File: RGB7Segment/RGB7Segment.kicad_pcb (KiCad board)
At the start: 2 copper layers, 38.5 x 25.5 mm, 21 parts, among them J1 Conn_01x02_Socket, J2 Conn_01x02_Socket

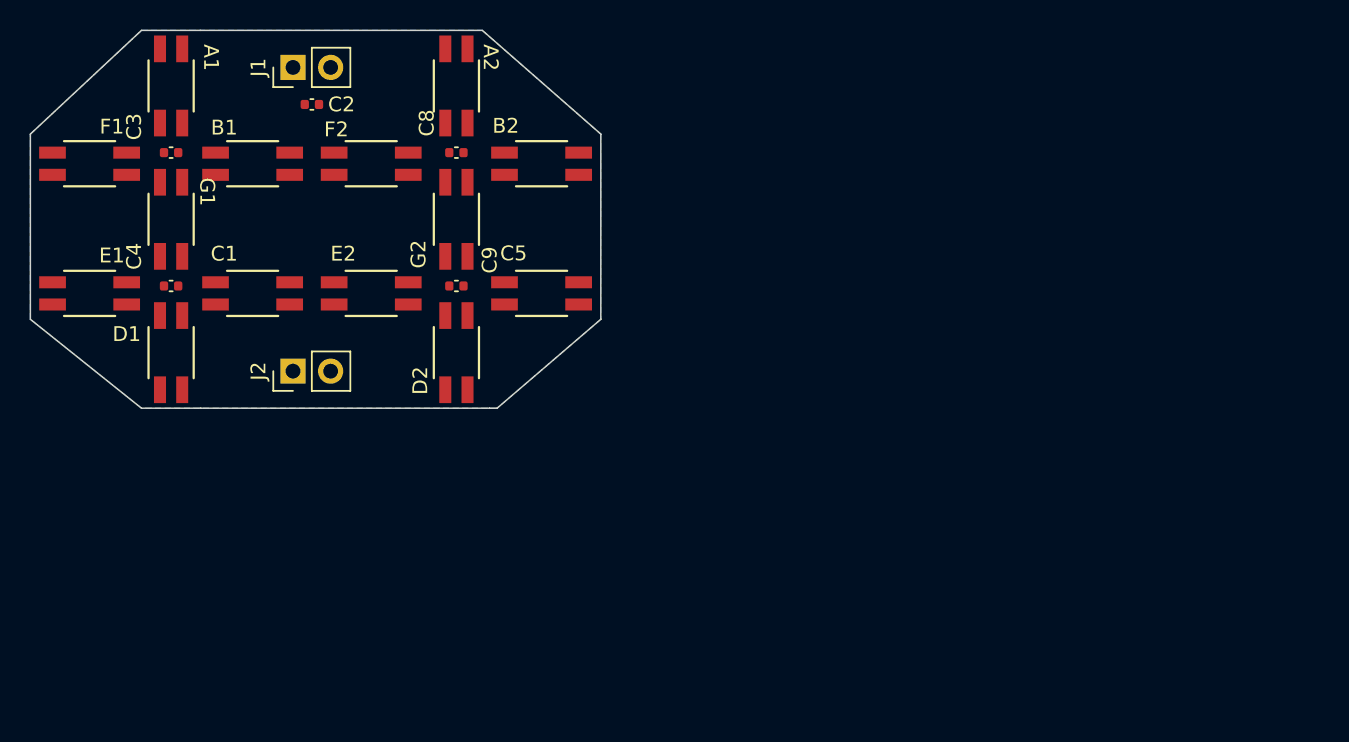
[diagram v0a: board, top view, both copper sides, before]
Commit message: Adding base parts / positioning.
Needs further alignment for horizontal vs Verticle SKU
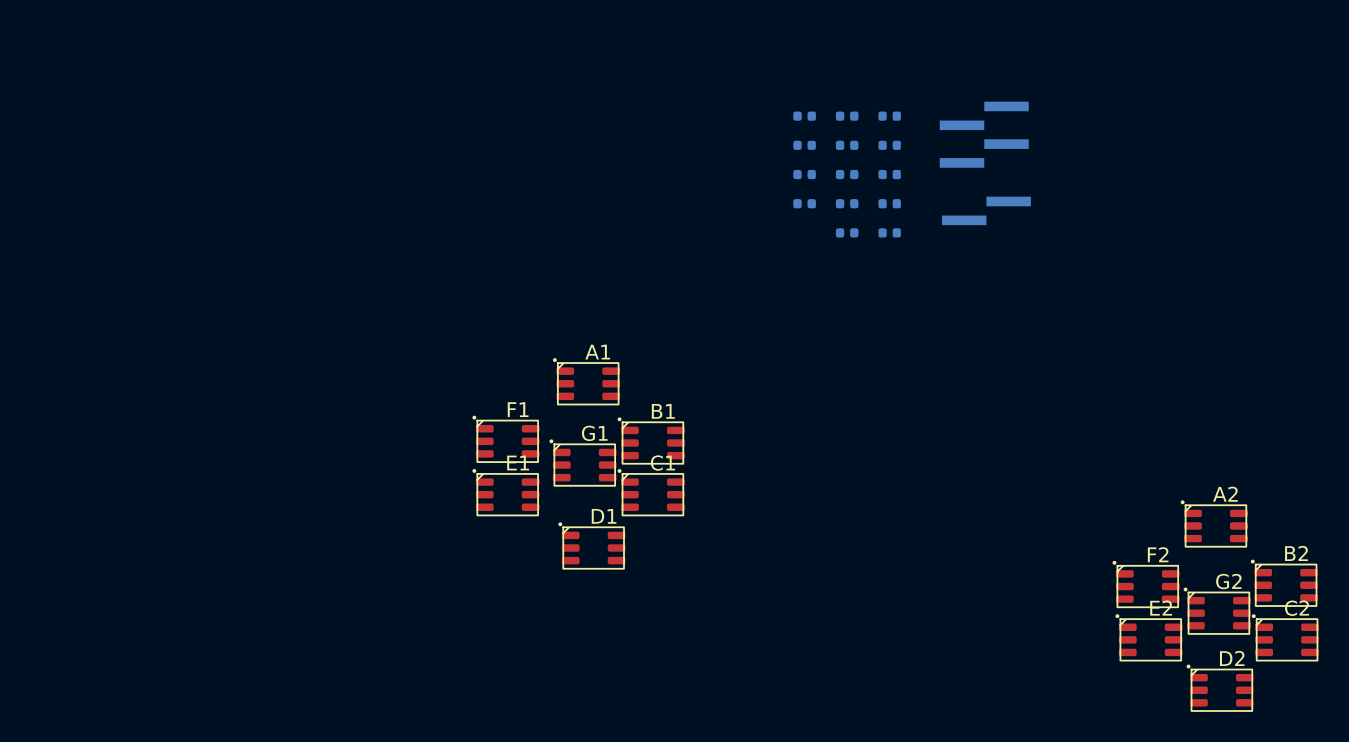
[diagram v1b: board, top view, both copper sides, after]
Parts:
- removed C3, C4, C8, C9: 0.1u, Capacitor_SMD:C_0402_1005Metric
- removed C5: SK6812-E, Library:4960_Test4
- added C10: 0.1u, Capacitor_SMD:C_0402_1005Metric, B.Cu at (247.5, 82.8)
- added C11: 0.1u, Capacitor_SMD:C_0402_1005Metric, B.Cu at (247.5, 84.8)
- added C12: 0.1u, Capacitor_SMD:C_0402_1005Metric, B.Cu at (247.5, 86.7)
- added C13: 0.1u, Capacitor_SMD:C_0402_1005Metric, B.Cu at (247.5, 88.7)
- added C14: 0.1u, Capacitor_SMD:C_0402_1005Metric, B.Cu at (247.5, 90.7)
- added C15: 0.1u, Capacitor_SMD:C_0402_1005Metric, B.Cu at (244.6, 82.8)
- added C16: 0.1u, Capacitor_SMD:C_0402_1005Metric, B.Cu at (244.6, 84.8)
- added C17: 0.1u, Capacitor_SMD:C_0402_1005Metric, B.Cu at (244.6, 86.7)
- added C18: 0.1u, Capacitor_SMD:C_0402_1005Metric, B.Cu at (244.6, 88.7)
- added C19: 0.1u, Capacitor_SMD:C_0402_1005Metric, B.Cu at (244.6, 90.7)
- added C20: 0.1u, Capacitor_SMD:C_0402_1005Metric, B.Cu at (241.8, 82.8)
- added C21: 0.1u, Capacitor_SMD:C_0402_1005Metric, B.Cu at (241.8, 84.8)
- added C22: 0.1u, Capacitor_SMD:C_0402_1005Metric, B.Cu at (241.8, 86.7)
- added C23: 0.1u, Capacitor_SMD:C_0402_1005Metric, B.Cu at (241.8, 88.7)
- A1, A2, B1, B2, C1, D1, D2, E1, E2, F1, F2, G1, G2: value SK6812-E -> ~; footprint Library:4960_Test4 -> Library:587-2086-247F
- C2: value 0.470u -> ~; footprint Capacitor_SMD:C_0402_1005Metric -> Library:587-2086-247F
- J1: footprint Connector_PinHeader_2.54mm:PinHeader_1x02_P2.54mm_Vertical -> Connector_PinHeader_1.27mm:PinHeader_1x02_P1.27mm_Vertical_SMD_Pin1Left; moved to B.Cu
- J2: value Conn_01x02_Socket -> Conn_01x04_Pin; footprint Connector_PinHeader_2.54mm:PinHeader_1x02_P2.54mm_Vertical -> Connector_PinHeader_1.27mm:PinHeader_1x04_P1.27mm_Vertical_SMD_Pin1Left; moved to B.Cu
- moved C2 73.3 mm to (272.8, 117.3), turned to 0 degrees
- moved F2 57.9 mm to (263.4, 113.7)
- moved A2 57.5 mm to (268.0, 109.6), turned to 0 degrees
- moved G2 56.2 mm to (268.2, 115.5), turned to 0 degrees
- moved B2 56.0 mm to (272.7, 113.6)
- moved E2 55.8 mm to (263.6, 117.3)
- moved D2 54.7 mm to (268.4, 120.7), turned to 0 degrees
- moved J2 49.3 mm to (253.9, 84.0), turned to 180 degrees
- moved J1 47.8 mm to (254.0, 89.2), turned to 180 degrees
- moved A1 32.8 mm to (225.6, 100.0), turned to 0 degrees
- moved F1 32.1 mm to (220.2, 103.9)
- moved B1 31.2 mm to (230.0, 104.0)
- moved G1 30.7 mm to (225.4, 105.5), turned to 0 degrees
- moved D1 29.7 mm to (226.0, 111.1), turned to 0 degrees
- moved E1 29.6 mm to (220.2, 107.5)
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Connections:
- A1 pad 1: VCC -> unconnected-(A1-DIN-Pad1)
- A1 pad 4: unconnected-(A1-DIN-Pad4) -> /A1_CO
- A2 pad 1: VCC -> unconnected-(A2-DIN-Pad1)
- A2 pad 4: unconnected-(A2-DIN-Pad4) -> /A2_CO
- B1 pad 1: VCC -> unconnected-(B1-DIN-Pad1)
- B1 pad 4: unconnected-(B1-DIN-Pad4) -> /B1_CO
- B2 pad 1: VCC -> unconnected-(B2-DIN-Pad1)
- B2 pad 4: unconnected-(B2-DIN-Pad4) -> /B2_CO
- C1 pad 1: VCC -> unconnected-(C1-DIN-Pad1)
- C1 pad 4: /DIN -> /C1_CO
- C2 pad 1: VCC -> unconnected-(C2-DIN-Pad1)
- C2 pad 2: GND -> unconnected-(C2-CIN-Pad2)
- D1 pad 1: VCC -> unconnected-(D1-DIN-Pad1)
- D1 pad 4: unconnected-(D1-DIN-Pad4) -> /D1_CO
- D2 pad 1: VCC -> unconnected-(D2-DIN-Pad1)
- D2 pad 4: unconnected-(D2-DIN-Pad4) -> /D2_CO
- E1 pad 1: VCC -> unconnected-(E1-DIN-Pad1)
- E1 pad 4: unconnected-(E1-DIN-Pad4) -> /E1_CO
- E2 pad 1: VCC -> unconnected-(E2-DIN-Pad1)
- E2 pad 2: /DOUT -> unconnected-(E2-CIN-Pad2)
- E2 pad 4: unconnected-(E2-DIN-Pad4) -> /E2_CO
- F1 pad 1: VCC -> unconnected-(F1-DIN-Pad1)
- F1 pad 4: unconnected-(F1-DIN-Pad4) -> /F1_CO
- F2 pad 1: VCC -> unconnected-(F2-DIN-Pad1)
- F2 pad 4: unconnected-(F2-DIN-Pad4) -> /F2_CO
- G1 pad 1: VCC -> unconnected-(G1-DIN-Pad1)
- G1 pad 4: unconnected-(G1-DIN-Pad4) -> /G1_CO
- G2 pad 1: VCC -> unconnected-(G2-DIN-Pad1)
- G2 pad 4: unconnected-(G2-DIN-Pad4) -> /G2_CO
- J2 pad 1: /DIN -> /COUT
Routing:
- net VCC: track 0.88 -> 0.00 mm
- removed copper zone on B.Cu, net GND
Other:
- board outline removed

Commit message: Adding Project Setup
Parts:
- moved A1 1.11 mm to (225.4, 101.1)
- moved D1 1.00 mm to (225.4, 110.3)
- moved E1 0.40 mm to (220.6, 107.5)
- moved F1 0.40 mm to (220.6, 103.9)
- moved B1 0.20 mm to (230.2, 104.0)
- moved C1 0.20 mm to (230.2, 107.5)
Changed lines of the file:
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@@
 		(at 225.365356 105.485356)
 		(property "Reference" "G1"
-			(at 2.25 -1.25 0)
+			(at 1.634644 0.914644 0)
 			(unlocked yes)
 			(layer "F.SilkS")
@@
 		(at 267.965356 109.6)
 		(property "Reference" "A2"
-			(at 2.25 -1.25 0)
+			(at 1.434644 1 0)
 			(unlocked yes)
 			(layer "F.SilkS")
@@
 	(footprint "Library:587-2086-247F"
 		(layer "F.Cu")
-		(at 229.965356 104)
+		(at 230.165356 104)
 		(property "Reference" "B1"
-			(at 2.25 -1.25 0)
+			(at 1.634644 0.8 0)
 			(unlocked yes)
 			(layer "F.SilkS")
@@
 		(at 272.765356 117.285356)
 		(property "Reference" "C2"
-			(at 2.25 -1.25 0)
+			(at 1.634644 0.914644 0)
 			(unlocked yes)
 			(layer "F.SilkS")
@@
 		(at 272.7 113.6)
 		(property "Reference" "B2"
-			(at 2.25 -1.25 0)
+			(at 1.5 1 0)
 			(unlocked yes)
 			(layer "F.SilkS")
@@
 		(at 263.565356 117.285356)
 		(property "Reference" "E2"
-			(at 2.25 -1.25 0)
+			(at 1.434644 0.914644 0)
 			(unlocked yes)
 			(layer "F.SilkS")
@@
 		(at 268.165356 115.485356)
 		(property "Reference" "G2"
-			(at 2.25 -1.25 0)
+			(at 1.634644 0.914644 0)
 			(unlocked yes)
 			(layer "F.SilkS")
@@
 	(footprint "Library:587-2086-247F"
 		(layer "F.Cu")
-		(at 229.965356 107.485356)
+		(at 230.165356 107.485356)
 		(property "Reference" "C1"
-			(at 2.25 -1.25 0)
+			(at 1.634644 0.714644 0)
 			(unlocked yes)
 			(layer "F.SilkS")
@@
 	(footprint "Library:587-2086-247F"
 		(layer "F.Cu")
-		(at 225.6 100)
+		(at 225.365356 101.085356)
 		(property "Reference" "A1"
-			(at 2.25 -1.25 0)
+			(at 1.634644 0.914644 0)
 			(unlocked yes)
 			(layer "F.SilkS")
@@
 	(footprint "Library:587-2086-247F"
 		(layer "F.Cu")
-		(at 220.165356 107.485356)
+		(at 220.565356 107.485356)
 		(property "Reference" "E1"
-			(at 2.25 -1.25 0)
+			(at 1.634644 0.714644 0)
 			(unlocked yes)
 			(layer "F.SilkS")
@@
 	(footprint "Library:587-2086-247F"
 		(layer "F.Cu")
-		(at 220.165356 103.885356)
+		(at 220.565356 103.885356)
 		(property "Reference" "F1"
-			(at 2.25 -1.25 0)
+			(at 1.634644 0.914644 0)
 			(unlocked yes)
 			(layer "F.SilkS")
@@
 	(footprint "Library:587-2086-247F"
 		(layer "F.Cu")
-		(at 225.965356 111.085356)
+		(at 225.365356 110.285356)
 		(property "Reference" "D1"
-			(at 2.25 -1.25 0)
+			(at 1.634644 0.914644 0)
 			(unlocked yes)
 			(layer "F.SilkS")
@@
 		(at 263.365356 113.685356)
 		(property "Reference" "F2"
-			(at 2.25 -1.25 0)
+			(at 1.634644 0.914644 0)
 			(unlocked yes)
 			(layer "F.SilkS")
@@
 		(at 268.365356 120.685356)
 		(property "Reference" "D2"
-			(at 2.25 -1.25 0)
-			(unlocked yes)
-			(layer "F.SilkS")
+			(at 1.634644 0.914644 0)
+			(unlocked yes)
+			(layer "F.SilkS")

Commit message: Standard push of SW in progress
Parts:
- moved A1 0.40 mm to (225.4, 101.5)
- moved D1 0.40 mm to (225.4, 109.9)
- moved E1 0.20 mm to (220.4, 107.5)
- moved F1 0.20 mm to (220.4, 103.9)
- moved G1 0.20 mm to (225.4, 105.7)
- moved B1 0.20 mm to (230.4, 104.0)
- moved C1 0.20 mm to (230.4, 107.5)
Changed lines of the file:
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@@
 	(footprint "Library:587-2086-247F"
 		(layer "F.Cu")
-		(at 225.365356 105.485356)
+		(at 225.365356 105.685356)
 		(property "Reference" "G1"
 			(at 1.634644 0.914644 0)
@@
 	(footprint "Library:587-2086-247F"
 		(layer "F.Cu")
-		(at 230.165356 104)
+		(at 230.365356 104)
 		(property "Reference" "B1"
 			(at 1.634644 0.8 0)
@@
 	(footprint "Library:587-2086-247F"
 		(layer "F.Cu")
-		(at 230.165356 107.485356)
+		(at 230.365356 107.485356)
 		(property "Reference" "C1"
 			(at 1.634644 0.714644 0)
@@
 	(footprint "Library:587-2086-247F"
 		(layer "F.Cu")
-		(at 225.365356 101.085356)
+		(at 225.365356 101.485356)
 		(property "Reference" "A1"
 			(at 1.634644 0.914644 0)
@@
 	(footprint "Library:587-2086-247F"
 		(layer "F.Cu")
-		(at 220.565356 107.485356)
+		(at 220.365356 107.485356)
 		(property "Reference" "E1"
 			(at 1.634644 0.714644 0)
@@
 	(footprint "Library:587-2086-247F"
 		(layer "F.Cu")
-		(at 220.565356 103.885356)
+		(at 220.365356 103.885356)
 		(property "Reference" "F1"
 			(at 1.634644 0.914644 0)
@@
 	(footprint "Library:587-2086-247F"
 		(layer "F.Cu")
-		(at 225.365356 110.285356)
+		(at 225.365356 109.885356)
 		(property "Reference" "D1"
 			(at 1.634644 0.914644 0)

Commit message: Initial Horizontal Placement
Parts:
- J1: footprint Connector_PinHeader_1.27mm:PinHeader_1x02_P1.27mm_Vertical_SMD_Pin1Left -> Connector_PinHeader_1.27mm:PinHeader_1x02_P1.27mm_Vertical; moved to F.Cu
- J2: footprint Connector_PinHeader_1.27mm:PinHeader_1x04_P1.27mm_Vertical_SMD_Pin1Left -> Connector_PinHeader_1.27mm:PinHeader_1x04_P1.27mm_Vertical; moved to F.Cu
- moved J2 43.2 mm to (218.2, 108.4)
- moved C11 34.4 mm to (221.8, 107.6), turned to 45 degrees
- moved C10 34.1 mm to (221.8, 105.2), turned to -135 degrees
- moved C12 31.0 mm to (226.8, 109.8), turned to 45 degrees
- moved F2 29.4 mm to (235.6, 104.0)
- moved G2 29.3 mm to (240.6, 105.5)
- moved B2 28.8 mm to (245.6, 104.0)
- moved A2 28.5 mm to (240.6, 101.5)
- moved C20 28.3 mm to (226.8, 106.8), turned to -135 degrees
- moved C15 26.8 mm to (226.8, 102.8), turned to -135 degrees
- moved D2 26.4 mm to (243.7, 111.2), turned to 180 degrees
- moved E2 26.2 mm to (238.7, 109.0), turned to 180 degrees
- moved C2 25.5 mm to (248.7, 109.0), turned to 180 degrees
- moved C17 24.5 mm to (231.8, 107.6), turned to 45 degrees
- moved C16 24.2 mm to (237.1, 107.7), turned to 45 degrees
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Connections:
- A1 pad 1: unconnected-(A1-DIN-Pad1) -> /G1_DO
- A1 pad 2: unconnected-(A1-CIN-Pad2) -> /G1_CO
- A2 pad 1: unconnected-(A2-DIN-Pad1) -> /F2_DO
- A2 pad 2: unconnected-(A2-CIN-Pad2) -> /F2_CO
- B1 pad 1: unconnected-(B1-DIN-Pad1) -> /A1_DO
- B1 pad 2: unconnected-(B1-CIN-Pad2) -> /A1_CO
- B2 pad 1: unconnected-(B2-DIN-Pad1) -> /G2_DO
- B2 pad 2: unconnected-(B2-CIN-Pad2) -> /G2_CO
- C1 pad 1: unconnected-(C1-DIN-Pad1) -> /E2_DO
- C1 pad 2: unconnected-(C1-CIN-Pad2) -> /E2_CO
- C2 pad 1: unconnected-(C2-DIN-Pad1) -> /B2_DO
- C2 pad 2: unconnected-(C2-CIN-Pad2) -> /B2_CO
- D1 pad 1: unconnected-(D1-DIN-Pad1) -> /C1_DO
- D1 pad 2: unconnected-(D1-CIN-Pad2) -> /C1_CO
- D2 pad 1: unconnected-(D2-DIN-Pad1) -> /C2_DO
- D2 pad 2: unconnected-(D2-CIN-Pad2) -> /C2_CO
- E1 pad 1: unconnected-(E1-DIN-Pad1) -> /D1_DO
- E1 pad 2: unconnected-(E1-CIN-Pad2) -> /D1_CO
- E1 pad 4: /E1_CO -> /COUT
- E1 pad 6: /E1_DO -> /DOUT
- E2 pad 1: unconnected-(E2-DIN-Pad1) -> /D2_DO
- E2 pad 2: unconnected-(E2-CIN-Pad2) -> /D2_CO
- F1 pad 1: unconnected-(F1-DIN-Pad1) -> /DIN
- F1 pad 2: unconnected-(F1-CIN-Pad2) -> /CIN
- F2 pad 1: unconnected-(F2-DIN-Pad1) -> /B1_DO
- F2 pad 2: unconnected-(F2-CIN-Pad2) -> /B1_CO
- G1 pad 1: unconnected-(G1-DIN-Pad1) -> /F1_DO
- G1 pad 2: unconnected-(G1-CIN-Pad2) -> /F1_CO
- G2 pad 1: unconnected-(G2-DIN-Pad1) -> /A2_DO
- G2 pad 2: unconnected-(G2-CIN-Pad2) -> /A2_CO
- J2 pad 1: /COUT -> /DOUT
- J2 pad 2: /DOUT -> /COUT
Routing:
- net /A2_DO: track 0.00 -> 0.60 mm

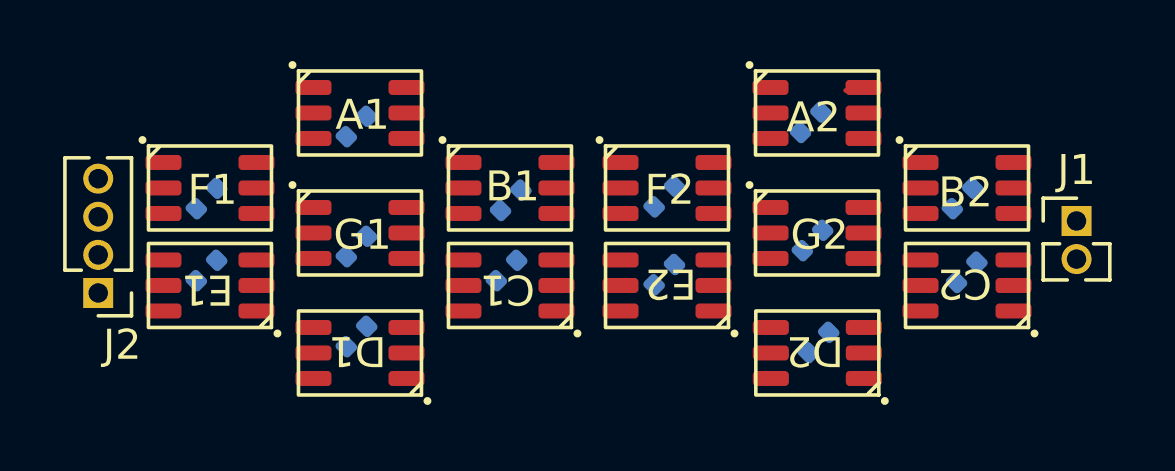
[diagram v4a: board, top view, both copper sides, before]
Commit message: Submitted RGB 7 Segment Layout
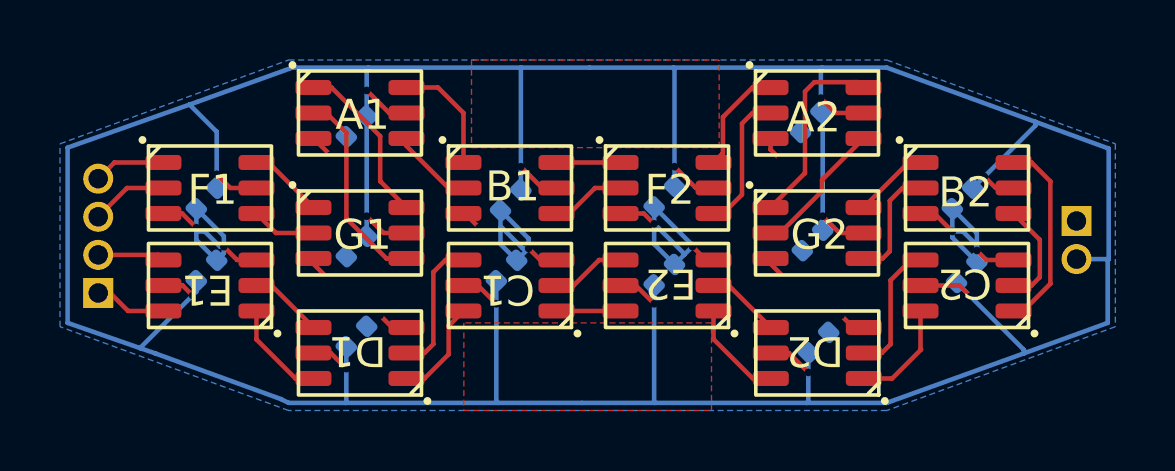
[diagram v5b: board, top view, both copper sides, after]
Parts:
- J1, J2: moved to B.Cu
- turned J1 to 180 degrees
- turned J2 to 0 degrees
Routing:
- net VCC: track 0.00 -> 148.3 mm, vias 0 -> 14
- net GND: track 0.00 -> 36.7 mm, vias 0 -> 30
- net /G1_CO: track 0.00 -> 6.78 mm
- net /B2_DO: track 0.00 -> 6.51 mm
- net /A2_DO: track 0.60 -> 6.49 mm
- net /G1_DO: track 0.00 -> 5.64 mm
- net /F2_CO: track 0.00 -> 4.68 mm
- net /A2_CO: track 0.00 -> 4.62 mm
- net /C1_CO: track 0.00 -> 4.59 mm
- net /C2_CO: track 0.00 -> 4.42 mm
- net /A1_DO: track 0.00 -> 3.90 mm
- net /G2_CO: track 0.00 -> 3.86 mm
- net /F2_DO: track 0.00 -> 3.64 mm
- net /C2_DO: track 0.00 -> 3.60 mm
- net /B2_CO: track 0.00 -> 3.48 mm
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- added copper zone on B.Cu, net GND
- added copper zone on F.Cu, net GND
